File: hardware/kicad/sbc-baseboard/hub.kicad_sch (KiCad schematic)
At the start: 88 parts, among them J1 USB-C upstream, J4 USB-A PORT1, J5 USB-A PORT3, U401 USBLC6-2SC6, U402 USB2517, U403 TPS2553DBV, U404 TPS2553DBV, U405 TPS2553DBV, U406 TPS2553DBV, U407 TPS2553DBV, U408 USBLC6-2SC6, U409 USBLC6-2SC6, U410 USBLC6-2SC6, U411 USBLC6-2SC6, Y401 24MHz

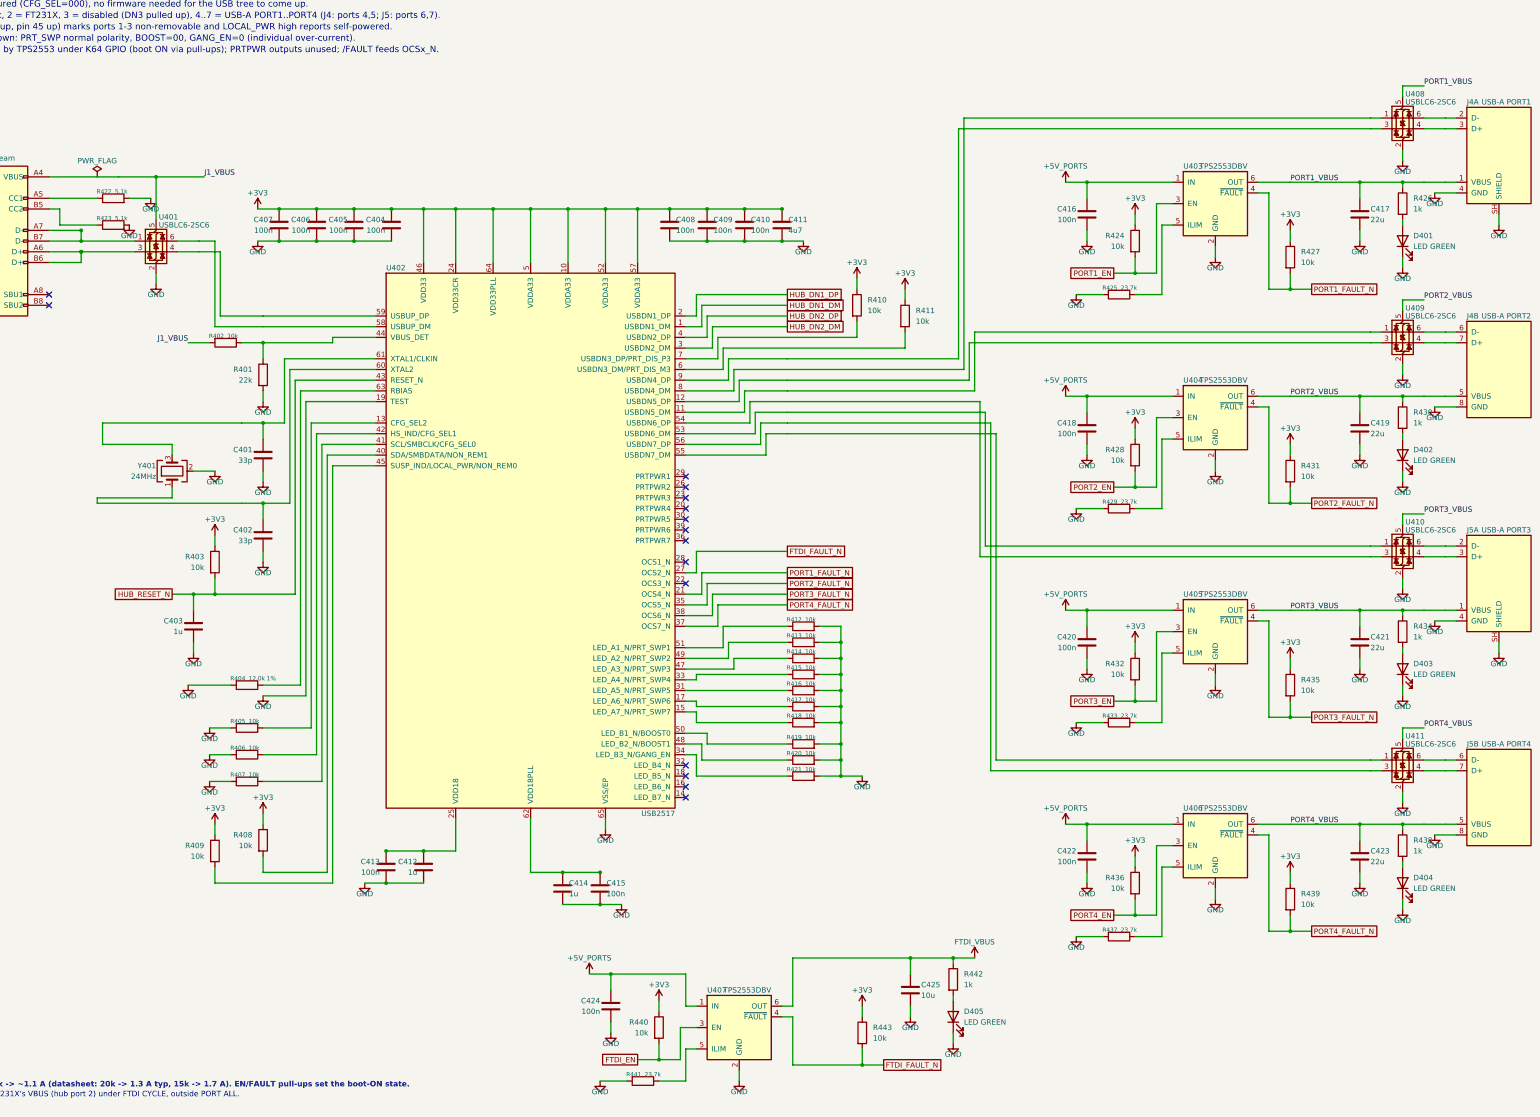
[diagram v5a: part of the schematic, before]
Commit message: Reference-design review; pin numbers and real text widths in the layout gate
Review (docs/reference-design-review.md): every IC's surrounding parts
compared with its datasheet typical application or evaluation board.
Brought in line:
- TPS54560B compensation 16.9k / 4.7 nF / 47 pF (the 5 V / 400 kHz design
  example, same 141 uF ceramic output); the placeholders are gone.
- TPS62823 divider 453k / 100k with the 120 pF feed-forward capacitor the
  datasheet recommends.
- USB2517 VBUS_DET from the EVB: 100k / 100k with 1 uF (was 10k / 22k, 3.4 V
  at a 3.3 V pin).
- KSZ8081 MDIO pull-up 1.0k as the datasheet requires (was 4.7k).
- FT231X: 27 R in series and 47 pF on USBDM/USBDP, datasheet figure 6.1.
Deviations kept and documented: the bucks' EN gated by the PD controller
instead of a UVLO divider, the FT231X fed by a power switch instead of a
ferrite bead, translator OE tied to the target rail.

Layout gate: pin numbers are text boxes like any other, and all text widths
come from a per-glyph table fitted to the extents KiCad writes into its PDF
(check_pins.py); the generator's spacing uses the same table. That exposed
and fixed: reference/value overlaps on narrow symbols (now stacked), rail
names printed over each other (the lane end and hanging pull-up now carry
half the rail name), a port-switch value over its pin number, turned parts
with text on the pin side, lane stacks whose spread collapsed at the grid
snap, routes landing on connector pin stubs (J16, J601, J14, D202 moved),
the PD controller's I2C and gate routes that crossed half the sheet (now
labels), and the port /FAULT and I2C1 pull-ups, which as hanging resistors
staggered off the sheet and are now one column to one +3V3 symbol. The
port switch carries FAULT above OUT so the switched rail's parts hang below
the label; the VBUS row is drawn from the connector back to the switch.

All sheets: ERC 0, contacts 0, merges 0, layout 0 in every category.
Connectivity against 8579cd2 differs only in the value ch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
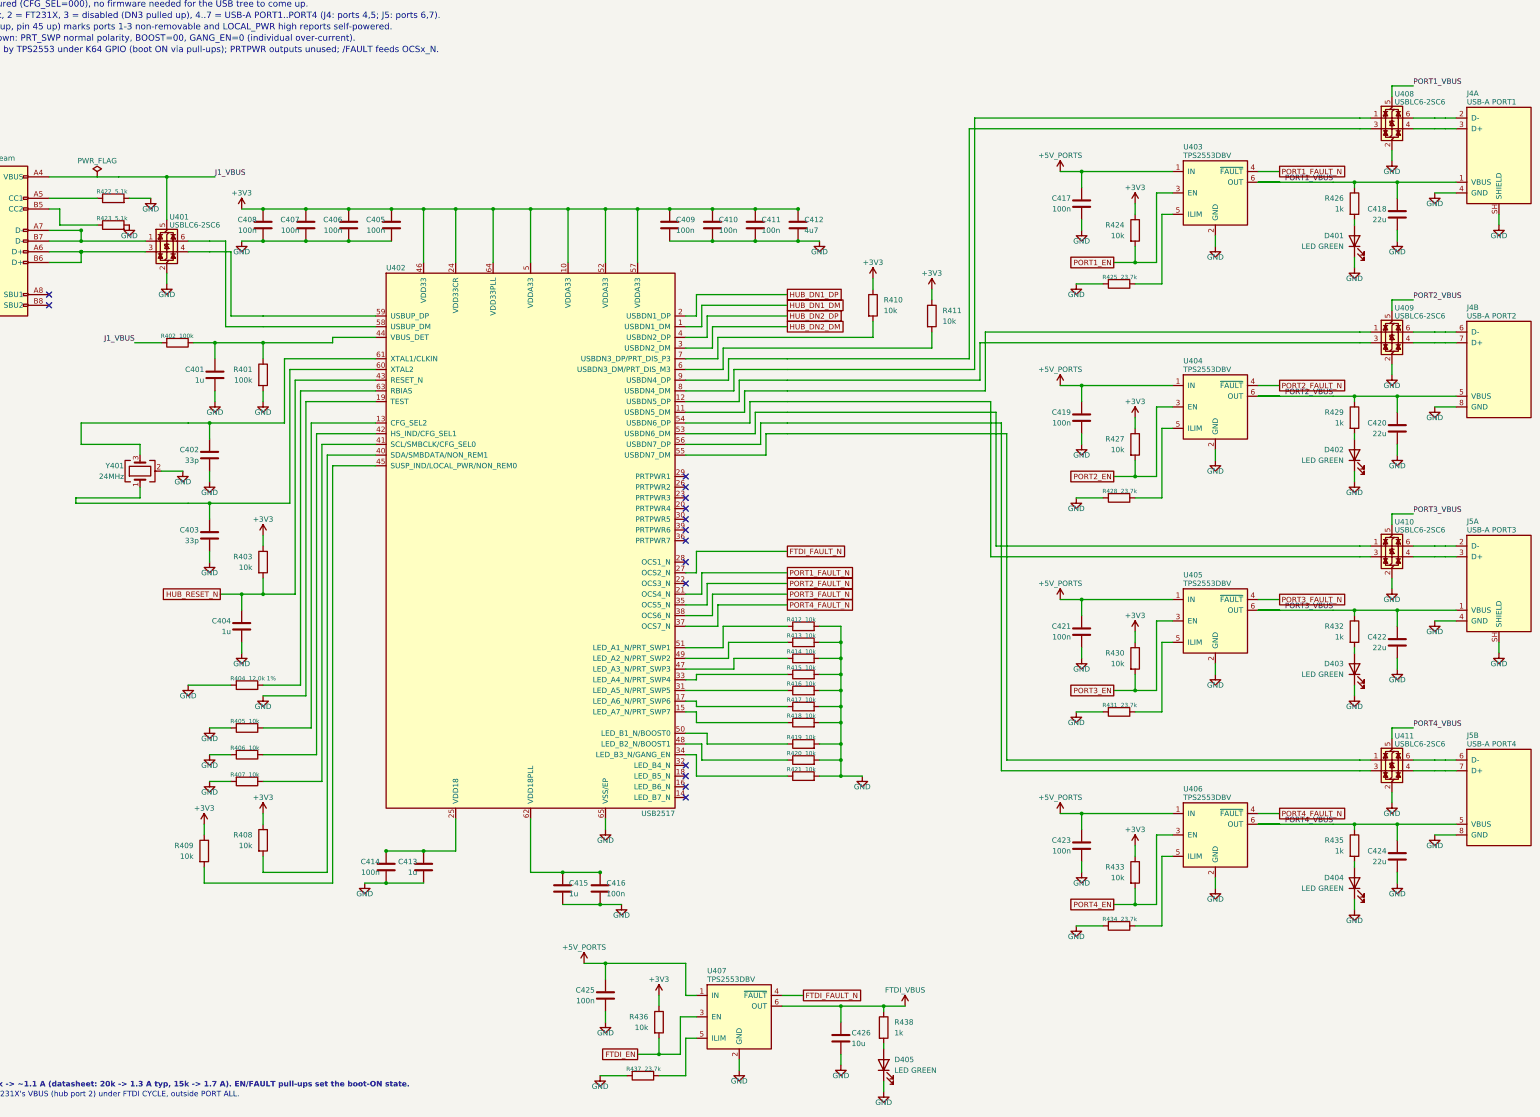
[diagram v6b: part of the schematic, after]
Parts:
- removed R439, R440, R443: 10k, Resistor_SMD:R_0603_1608Metric, symbol Device:R
- removed R441: 23.7k, Resistor_SMD:R_0603_1608Metric, symbol Device:R
- removed R442: 1k, Resistor_SMD:R_0603_1608Metric, symbol Device:R
- added C426: 10u, Capacitor_SMD:C_0805_2012Metric, symbol Device:C
- C401: value 33p -> 1u
- C403: value 1u -> 33p
- C404, C413, C415: value 100n -> 1u
- C411: value 4u7 -> 100n; footprint Capacitor_SMD:C_0805_2012Metric -> Capacitor_SMD:C_0603_1608Metric
- C412: value 1u -> 4u7; footprint Capacitor_SMD:C_0603_1608Metric -> Capacitor_SMD:C_0805_2012Metric
- C414: value 1u -> 100n
- C417, C419, C421, C423: value 22u -> 100n; footprint Capacitor_SMD:C_1206_3216Metric -> Capacitor_SMD:C_0603_1608Metric
- C418, C420, C422, C424: value 100n -> 22u; footprint Capacitor_SMD:C_0603_1608Metric -> Capacitor_SMD:C_1206_3216Metric
- C425: value 10u -> 100n; footprint Capacitor_SMD:C_0805_2012Metric -> Capacitor_SMD:C_0603_1608Metric
- R401: value 22k -> 100k
- R402: value 10k -> 100k
- R428, R431: value 10k -> 23.7k
- R429: value 23.7k -> 1k
- R430: value 1k -> 10k
- R432, R435: value 10k -> 1k
- R433: value 23.7k -> 10k
- R434: value 1k -> 23.7k
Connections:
- net +3V3: now also C412.1, R430.1, R433.1; no longer C404.1, R428.1, R431.1, R432.1, R435.1
- net +5V_PORTS: now also C417.1, C419.1, C421.1, C423.1, C425.1; no longer C416.1, C418.1, C420.1, C422.1, C424.1
- net FTDI_EN: now also R436.2
- net FTDI_VBUS: now also R438.1, C426.1; no longer C425.1
- net GND: now also R428.2, R431.2, R434.2, C426.2; no longer R429.2, R433.2
- net HUB_RESET_N: now also C404.1; no longer C403.1
- net PORT1_FAULT_N: no longer R427.2
- net PORT1_VBUS: now also C418.1; no longer C417.1
- net PORT2_EN: now also R427.2; no longer R428.2
- net PORT2_FAULT_N: no longer R431.2
- net PORT2_VBUS: now also C420.1, R429.1; no longer C419.1, R430.1
- net PORT3_EN: now also R430.2; no longer R432.2
- net PORT3_FAULT_N: no longer R435.2
- net PORT3_VBUS: now also C422.1, R432.1; no longer C421.1, R434.1
- net PORT4_EN: now also R433.2; no longer R436.2
- net PORT4_VBUS: now also C424.1, R435.1; no longer C423.1, R438.1
- net at U405.5 (ILIM): now also R431.1; no longer R433.1
- net at U404.5 (ILIM): now also R428.1; no longer R429.1
- net at C415.1, U402.62 (VDD18PLL): now also C416.1; no longer C414.1
- net at R401.1, R402.1, U402.44 (VBUS_DET): now also C401.1
- net at D403.2 (A): now also R432.2; no longer R434.2
- net at R437.1: now also U407.5 (ILIM); no longer U406.5 (ILIM)
- net at D405.2 (A): now also R438.2
- net at U402.60 (XTAL2), Y401.1: now also C403.1; no longer C402.1
- net at U402.61 (XTAL1/CLKIN), Y401.3: now also C402.1; no longer C401.1
- net at D404.2 (A): now also R435.2; no longer R438.2
- net at C413.1, U402.25 (VDD18): now also C414.1; no longer C412.1
- net at D402.2 (A): now also R429.2; no longer R430.2
- new net: R434.1, U406.5 (ILIM)
